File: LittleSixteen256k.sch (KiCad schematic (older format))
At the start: 6 parts, among them U5 MOS_6529, U6 74LS02, U7 74HCT02, U9 74HCT257

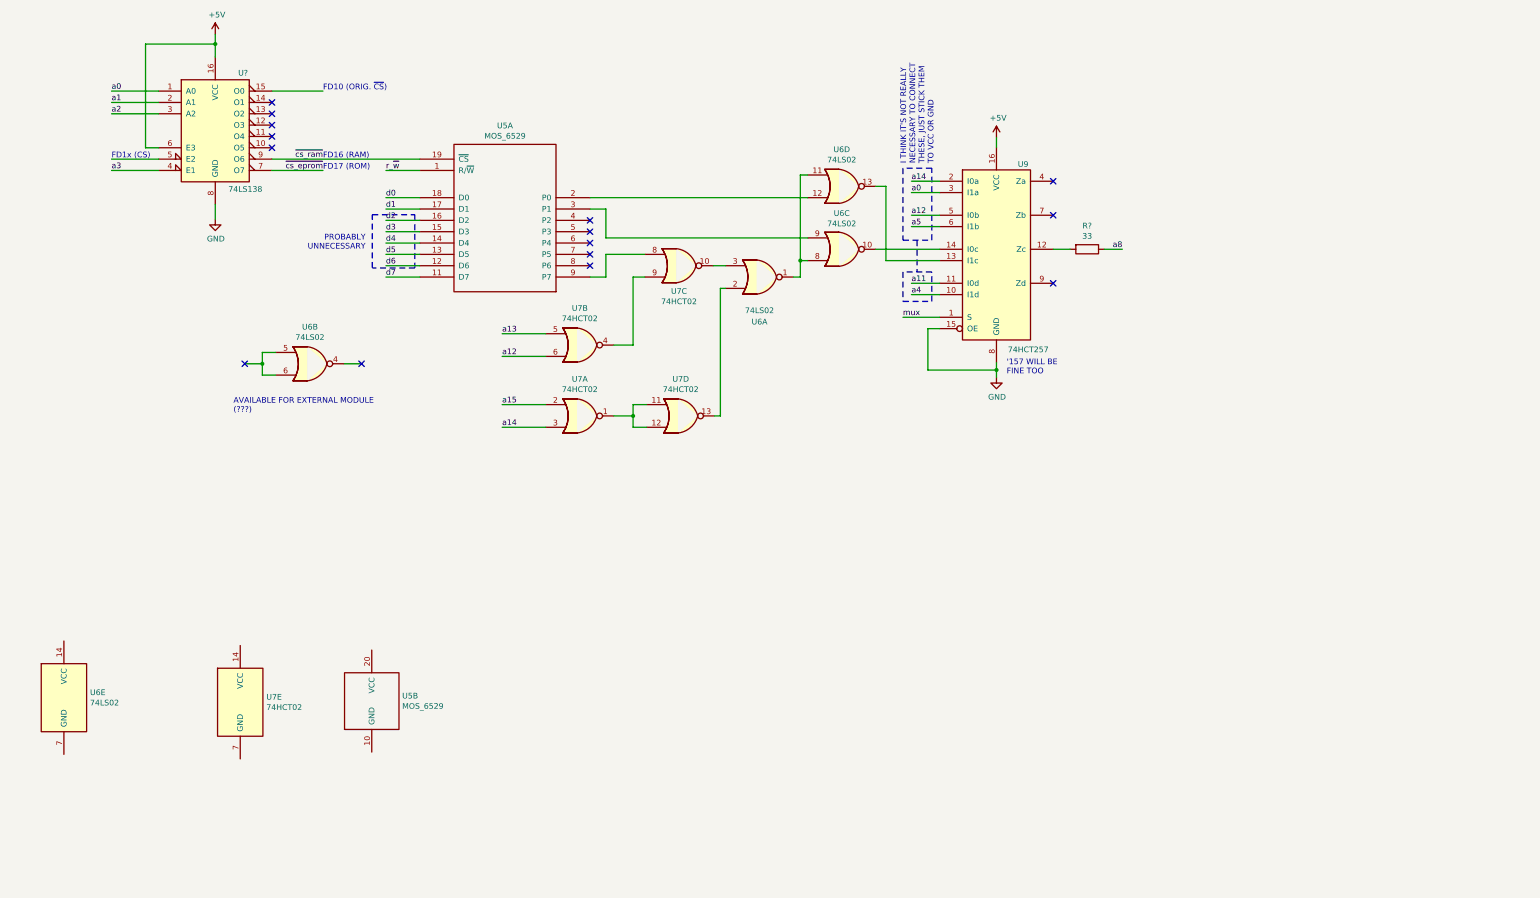
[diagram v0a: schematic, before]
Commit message: Add decoupling caps
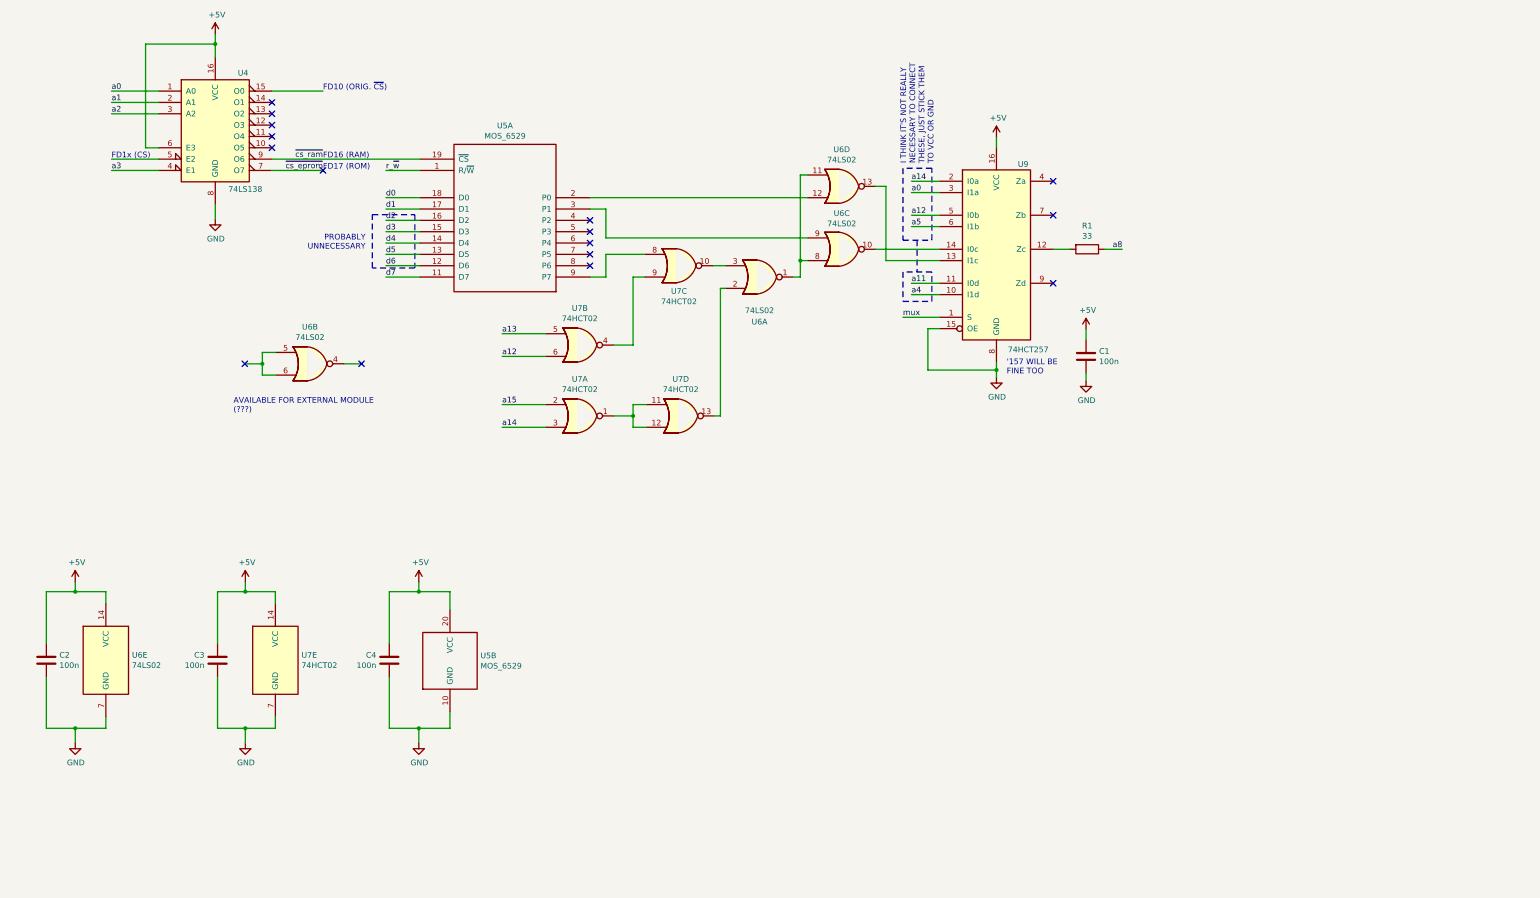
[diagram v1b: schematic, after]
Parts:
- added C1, C2, C3, C4: 100n, symbol Device:C
- gave numbers to parts that had none: 2
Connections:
- net +5V: now also U5.20 (VCC), U6.14 (VCC), U7.14 (VCC), C1.1, C2.1, C3.1, C4.1
- net GND: now also U5.10 (GND), U6.7 (GND), U7.7 (GND), C1.2, C2.2, C3.2, C4.2
- no-connect marks 15 -> 16
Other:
- moved on the sheet: U5B, U6E, U7E

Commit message: Apply "Update 1" introducing the "TED Feature" Restricts TED access to RAM bank 3 when the 6th bit of the RAM register is cleared.
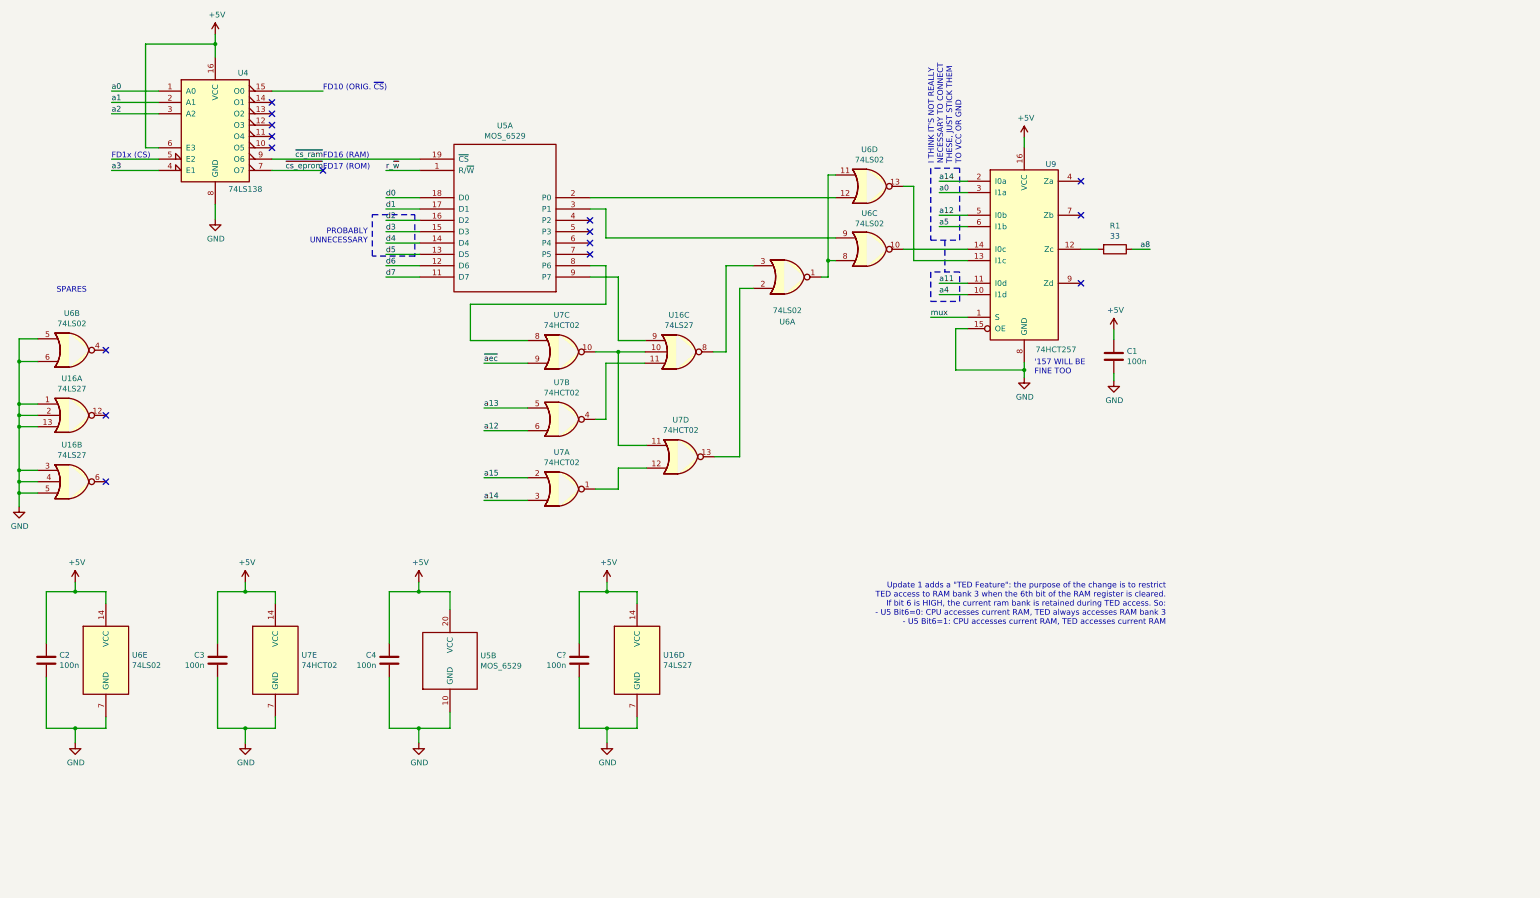
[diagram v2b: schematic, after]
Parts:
- added C?: 100n, symbol Device:C
- added U16: 74LS27, symbol 74xx:74LS27
- U5: footprint MODULE -> (none)
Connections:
- net +5V: now also C?.1, U16.14 (VCC)
- net GND: now also U6.5, U6.6, C?.2, U16.1, U16.13, U16.2, U16.3, U16.4, U16.5, U16.7 (GND)
- net at U6.3: now also U16.8; no longer U7.10
- net at U7.1, U7.12: no longer U7.11
- net at U7.4: now also U16.11; no longer U7.9
- net at U7.8: now also U5.8 (P6); no longer U5.9 (P7)
- new net: U16.10, U7.10, U7.11
- new net: U16.9, U5.9 (P7)
- new net ~aec: U7.9
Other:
- note added: "SPARES"
- note added: "Update 1 adds a "TED Feature": the purpose of the change is to restrict\nTED access to RAM bank 3 when the 6th bit of the RAM register is cleared.\nIf bit 6 is HIGH, the current ram bank is retained during TED access. So:\n- U5 Bit6=0: CPU accesses current RAM, TED always accesses RAM bank 3\n- U5 Bit6=1: CPU accesses current RAM, TED accesses current RAM"
- note removed: "AVAILABLE FOR EXTERNAL MODULE\n(???)"
- moved on the sheet: C1, R1, U6A, U6B, U6C, U6D, U7A, U7B, U7C, U7D, U9

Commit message: Hopefully we now have the schematics for a fully working internal RAM expansion
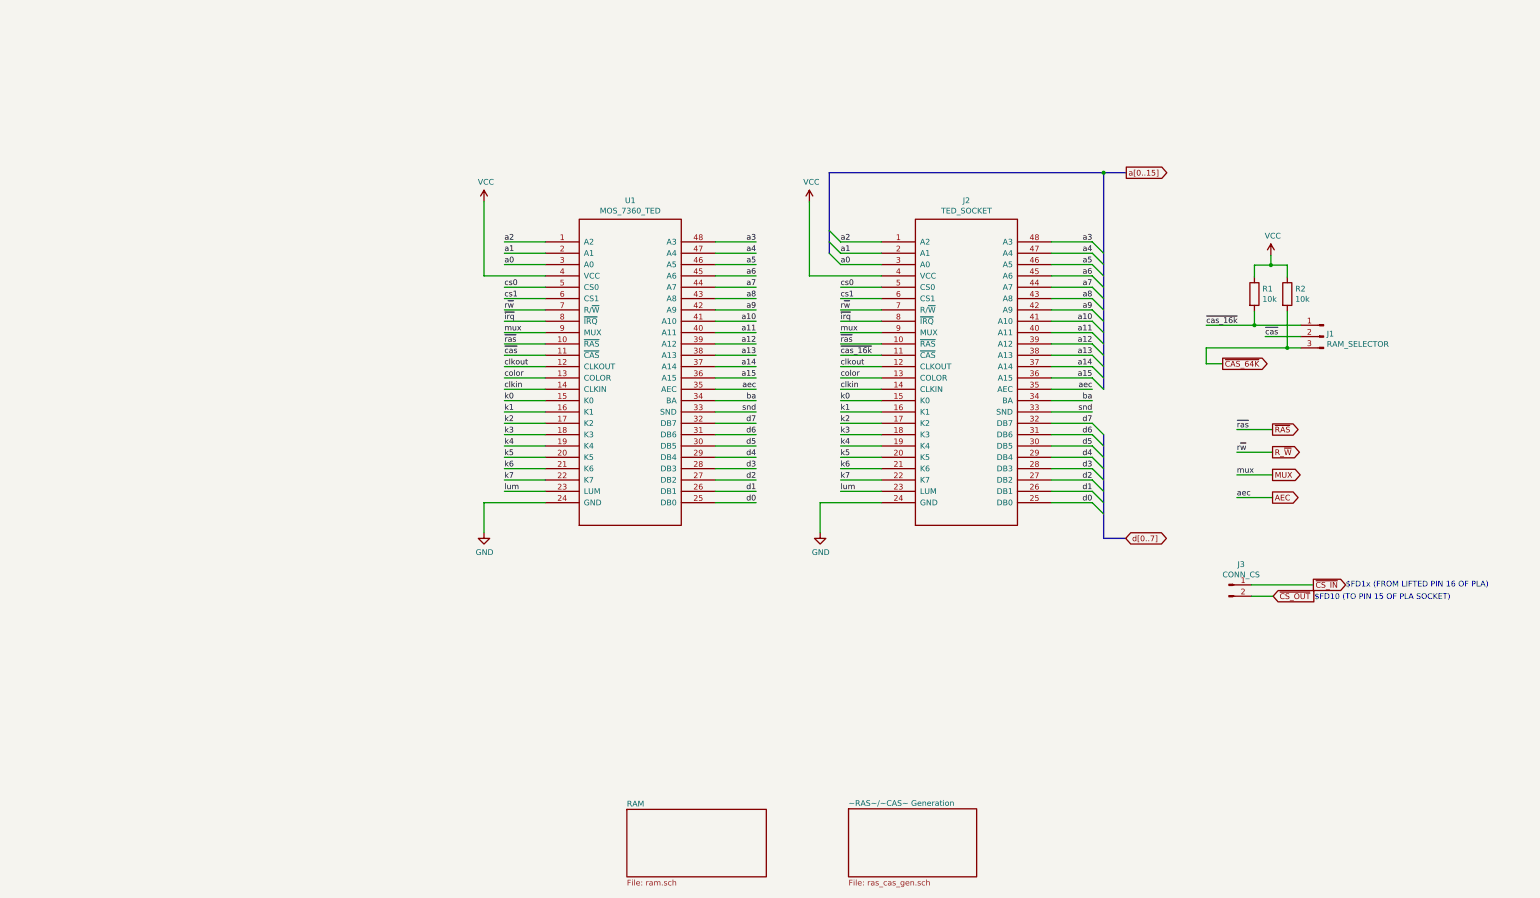
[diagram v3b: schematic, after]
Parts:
- removed C1, C2, C3, C4, C?: 100n, symbol Device:C
- removed U16: 74LS27, symbol 74xx:74LS27
- removed U4: 74LS138, symbol 74xx:74LS138
- removed U5: MOS_6529, symbol MOS_6529:MOS_6529
- removed U6: 74LS02, symbol 74xx:74LS02
- removed U7: 74HCT02, symbol 74xx:74HCT02
- removed U9: 74HCT257, symbol 74xx:74LS257
- added J1: RAM_SELECTOR, Fixteen:Pin_Header_Straight_1x03-ModSilkS, symbol Connector:Conn_01x03_Male
- added J2: TED_SOCKET, Fixteen:DIP-48_W15.24mm_LongPads_ModSilkS, symbol MOS_7360_TED:TED_SOCKET
- added J3: CONN_CS, symbol Connector:Conn_01x02_Male
- added R2: 10k, Resistor_SMD:R_0805_2012Metric_Pad1.20x1.40mm_HandSolder, symbol Device:R
- added U1: MOS_7360_TED, Package_DIP:DIP-48_W15.24mm_Socket_LongPads, symbol MOS_7360_TED:MOS_7360_TED
- R1: value 33 -> 10k; footprint (none) -> Resistor_SMD:R_0805_2012Metric_Pad1.20x1.40mm_HandSolder
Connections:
- net GND: now also J2.24 (GND), U1.24 (GND)
- net a0: now also J2.3 (A0), U1.3 (A0)
- net a1: now also J2.2 (A1), U1.2 (A1)
- net a11: now also J2.40 (A11), U1.40 (A11)
- net a12: now also J2.39 (A12), U1.39 (A12)
- net a13: now also J2.38 (A13), U1.38 (A13)
- net a14: now also J2.37 (A14), U1.37 (A14)
- net a15: now also J2.36 (A15), U1.36 (A15)
- net a2: now also J2.1 (A2), U1.1 (A2)
- net a3: now also J2.48 (A3), U1.48 (A3)
- net a4: now also J2.47 (A4), U1.47 (A4)
- net a5: now also J2.46 (A5), U1.46 (A5)
- net a8: now also J2.43 (A8), U1.43 (A8); no longer R1.1
- net d0: now also J2.25 (DB0), U1.25 (DB0)
- net d1: now also J2.26 (DB1), U1.26 (DB1)
- net d2: now also J2.27 (DB2), U1.27 (DB2)
- net d3: now also J2.28 (DB3), U1.28 (DB3)
- net d4: now also J2.29 (DB4), U1.29 (DB4)
- net d5: now also J2.30 (DB5), U1.30 (DB5)
- net d6: now also J2.31 (DB6), U1.31 (DB6)
- net d7: now also J2.32 (DB7), U1.32 (DB7)
- net ~cas_16k: now reaches R1.2
- net ~cas_16k: now also J1.1 (Pin_1), J2.11 (~CAS)
- new net AEC: J2.35 (AEC), U1.35 (AEC)
- new net MUX: J2.9 (MUX), U1.9 (MUX)
- new net R_~W: J2.7 (R/~W), U1.7 (R/~W)
- new net VCC: J2.4 (VCC), R1.1, R2.1, U1.4 (VCC)
- new net a10: J2.41 (A10), U1.41 (A10)
- new net a6: J2.45 (A6), U1.45 (A6)
- new net a7: J2.44 (A7), U1.44 (A7)
- new net a9: J2.42 (A9), U1.42 (A9)
- new net ba: J2.34 (BA), U1.34 (BA)
- new net clkin: J2.14 (CLKIN), U1.14 (CLKIN)
- new net clkout: J2.12 (CLKOUT), U1.12 (CLKOUT)
- new net color: J2.13 (COLOR), U1.13 (COLOR)
- new net cs0: J2.5 (CS0), U1.5 (CS0)
- new net cs1: J2.6 (CS1), U1.6 (CS1)
- new net k0: J2.15 (K0), U1.15 (K0)
- new net k1: J2.16 (K1), U1.16 (K1)
- new net k2: J2.17 (K2), U1.17 (K2)
- new net k3: J2.18 (K3), U1.18 (K3)
- new net k4: J2.19 (K4), U1.19 (K4)
- new net k5: J2.20 (K5), U1.20 (K5)
- new net k6: J2.21 (K6), U1.21 (K6)
- new net k7: J2.22 (K7), U1.22 (K7)
- new net lum: J2.23 (LUM), U1.23 (LUM)
- new net snd: J2.33 (SND), U1.33 (SND)
- new net ~CAS_64K: J1.3 (Pin_3), R2.2
- new net ~CS_IN: J3.1 (Pin_1)
- new net ~CS_OUT: J3.2 (Pin_2)
- new net ~RAS: J2.10 (~RAS), U1.10 (~RAS)
- new net ~cas: J1.2 (Pin_2), U1.11 (~CAS)
- new net ~irq: J2.8 (~IRQ), U1.8 (~IRQ)
- no-connect marks 16 -> 0
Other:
- note added: "$FD10 (TO PIN 15 OF PLA SOCKET)"
- note added: "$FD1x (FROM LIFTED PIN 16 OF PLA)"
- note removed: "'157 WILL BE\nFINE TOO"
- note removed: "FD10 (ORIG. ~CS~)"
- note removed: "FD16 (RAM)"
- note removed: "FD17 (ROM)"
- note removed: "FD1x (CS)"
- note removed: "I THINK IT'S NOT REALLY\nNECESSARY TO CONNECT\nTHESE, JUST STICK THEM\nTO VCC OR GND"
- note removed: "PROBABLY\nUNNECESSARY"
- note removed: "SPARES"
- note removed: "Update 1 adds a "TED Feature": the purpose of the change is to restrict\nTED access to RAM bank 3 when the 6th bit of the RAM register is cleared.\nIf bit 6 is HIGH, the current ram bank is retained during TED access. So:\n- U5 Bit6=0: CPU accesses current RAM, TED always accesses RAM bank 3\n- U5 Bit6=1: CPU accesses current RAM, TED accesses current RAM"

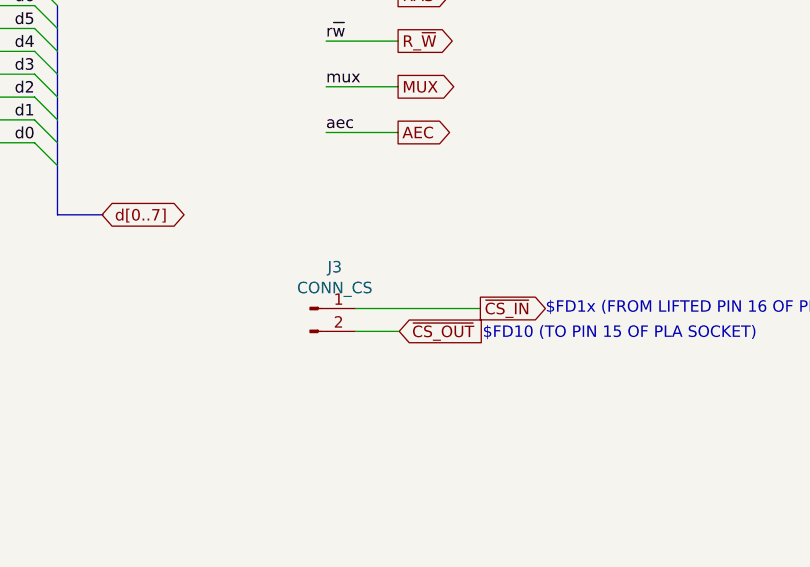
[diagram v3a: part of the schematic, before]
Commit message: Switch out the MOS 6529
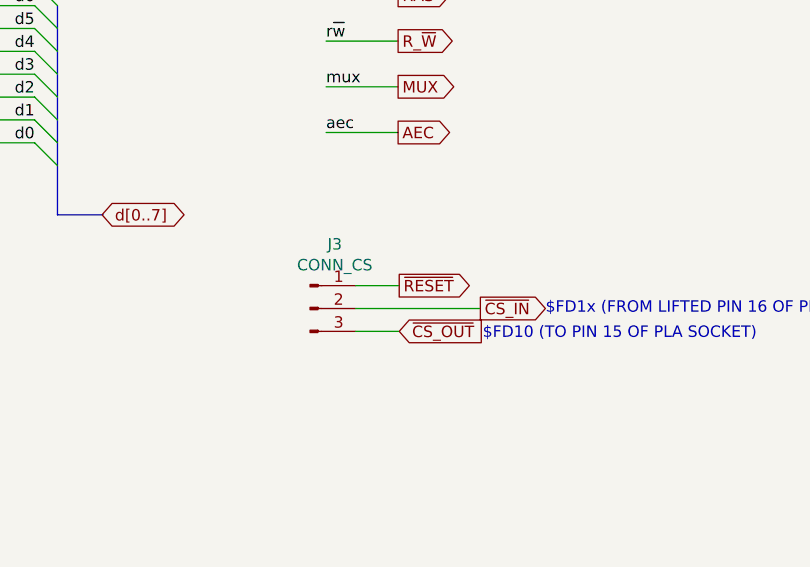
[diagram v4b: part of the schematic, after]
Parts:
- removed J3: CONN_CS, symbol Connector:Conn_01x02_Male
- added J3: CONN_CS, Connector_PinHeader_2.54mm:PinHeader_1x03_P2.54mm_Vertical, symbol Connector:Conn_01x03_Male
- J1: footprint Fixteen:Pin_Header_Straight_1x03-ModSilkS -> Connector_PinHeader_2.54mm:PinHeader_1x03_P2.54mm_Vertical
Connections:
- net ~CS_IN: now also J3.2 (Pin_2)
- net ~CS_OUT: now also J3.3 (Pin_3)
- new net ~RESET: J3.1 (Pin_1)
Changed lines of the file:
@@
 F 0 "J1" H 12337 3844 50  0000 R CNN
 F 1 "RAM_SELECTOR" H 12337 3753 50  0000 R CNN
-F 2 "Fixteen:Pin_Header_Straight_1x03-ModSilkS" H 12365 3820 50  0001 C CNN
+F 2 "Connector_PinHeader_2.54mm:PinHeader_1x03_P2.54mm_Vertical" H 12365 3820 50  0001 C CNN
 F 3 "~" H 12365 3820 50  0001 C CNN
 	1    12365 3820
@@
 Text GLabel 11915 5240 2    50   Output ~ 0
 AEC
-$Comp
-L Connector:Conn_01x02_Male J3
-U 1 1 63C6835C
-P 11530 6010
-F 0 "J3" H 11638 6191 50  0000 C CNN
-F 1 "CONN_CS" H 11638 6100 50  0000 C CNN
-F 2 "" H 11530 6010 50  0001 C CNN
-F 3 "~" H 11530 6010 50  0001 C CNN
-	1    11530 6010
-	1    0    0    -1
-$EndComp
 Text GLabel 12275 6010 2    50   Output ~ 0
 ~CS_IN
@@
 Text Notes 12285 6150 0    50   ~ 0
 $FD10 (TO PIN 15 OF PLA SOCKET)
+$Comp
+L Connector:Conn_01x03_Male J3
+U 1 1 63E0AE52
+P 11530 6010
+F 0 "J3" H 11638 6291 50  0000 C CNN
+F 1 "CONN_CS" H 11638 6200 50  0000 C CNN
+F 2 "Connector_PinHeader_2.54mm:PinHeader_1x03_P2.54mm_Vertical" H 11530 6010 50  0001 C CNN
+F 3 "~" H 11530 6010 50  0001 C CNN
+	1    11530 6010
+	1    0    0    -1
+$EndComp
+Wire Wire Line
+	11730 5910 11920 5910
+Text GLabel 11920 5910 2    50   Output ~ 0
+~RESET
 Wire Bus Line
 	8005 2375 8005 3085

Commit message: Start working on PCB
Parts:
- J1: renamed from J2; footprint Fixteen:DIP-48_W15.24mm_LongPads_ModSilkS -> Hannes256:DIP-48_W15.24mm_LongPads_ModSilkS
- renumbered J1 to J2
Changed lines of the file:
@@
 P 9215 4135
 AR Path="/62E48B71/639188CC" Ref="J?"  Part="1"
-AR Path="/639188CC" Ref="J2"  Part="1"
-F 0 "J2" H 9215 5650 50  0000 C CNN
+AR Path="/639188CC" Ref="J1"  Part="1"
+F 0 "J1" H 9215 5650 50  0000 C CNN
 F 1 "TED_SOCKET" H 9215 5559 50  0000 C CNN
-F 2 "Fixteen:DIP-48_W15.24mm_LongPads_ModSilkS" H 9215 4135 50  0001 C CNN
+F 2 "Hannes256:DIP-48_W15.24mm_LongPads_ModSilkS" H 9215 4135 50  0001 C CNN
 F 3 "DOCUMENTATION" H 9215 4135 50  0001 C CNN
 	1    9215 4135
@@
 P 12365 3820
 AR Path="/62E48B71/63918991" Ref="J?"  Part="1"
-AR Path="/63918991" Ref="J1"  Part="1"
-F 0 "J1" H 12337 3844 50  0000 R CNN
+AR Path="/63918991" Ref="J2"  Part="1"
+F 0 "J2" H 12337 3844 50  0000 R CNN
 F 1 "RAM_SELECTOR" H 12337 3753 50  0000 R CNN
 F 2 "Connector_PinHeader_2.54mm:PinHeader_1x03_P2.54mm_Vertical" H 12365 3820 50  0001 C CNN
